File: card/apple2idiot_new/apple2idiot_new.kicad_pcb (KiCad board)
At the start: 2 copper layers, 167.6 x 77.5 mm, 10 parts, among them J1 Computer goes here, J2 Conn_02x02_Odd_Even, J3 Conn_01x04, J4 Conn_02x02_Odd_Even, J5 Conn_02x02_Odd_Even, J6 Conn_02x07_Odd_Even, U1 IDT7132, U2 ESP32-DEVKITC-32D

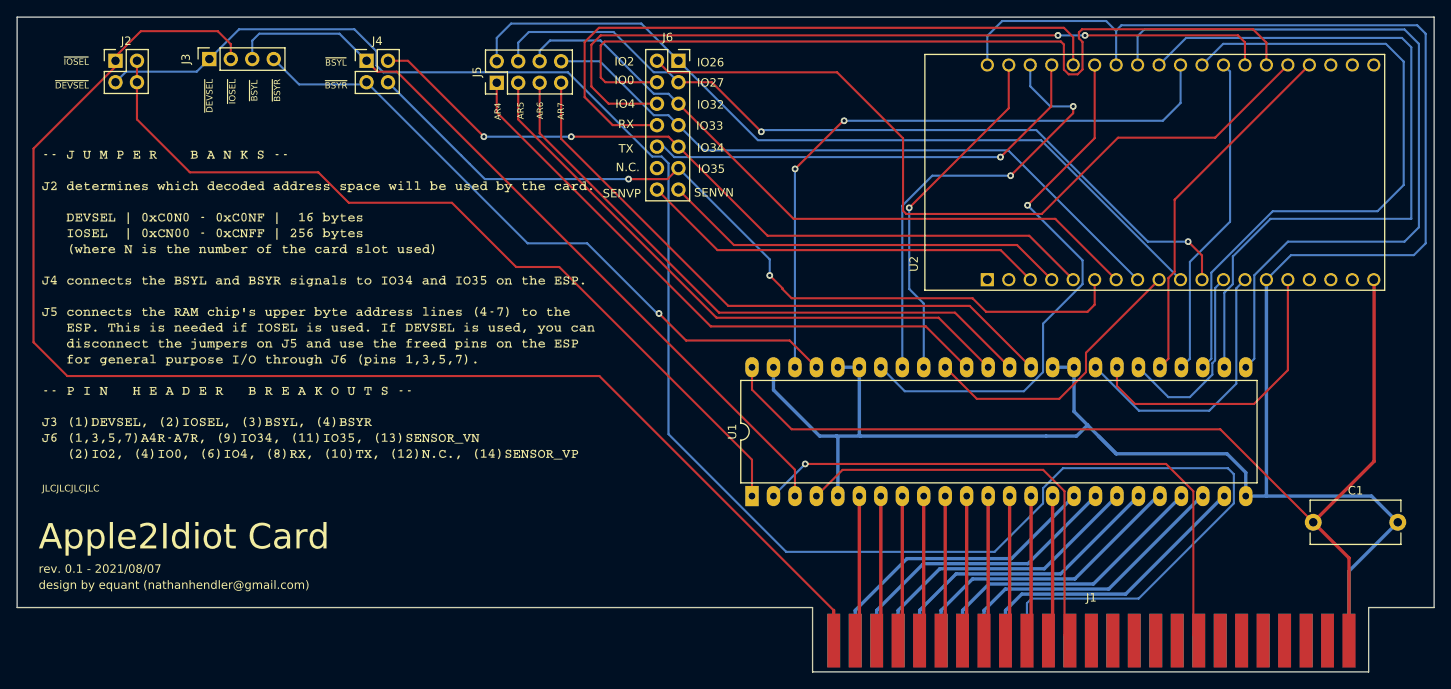
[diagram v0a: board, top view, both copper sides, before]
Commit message: Card work: Diode, no more DEVSEL support, A8-10 grounded, and more
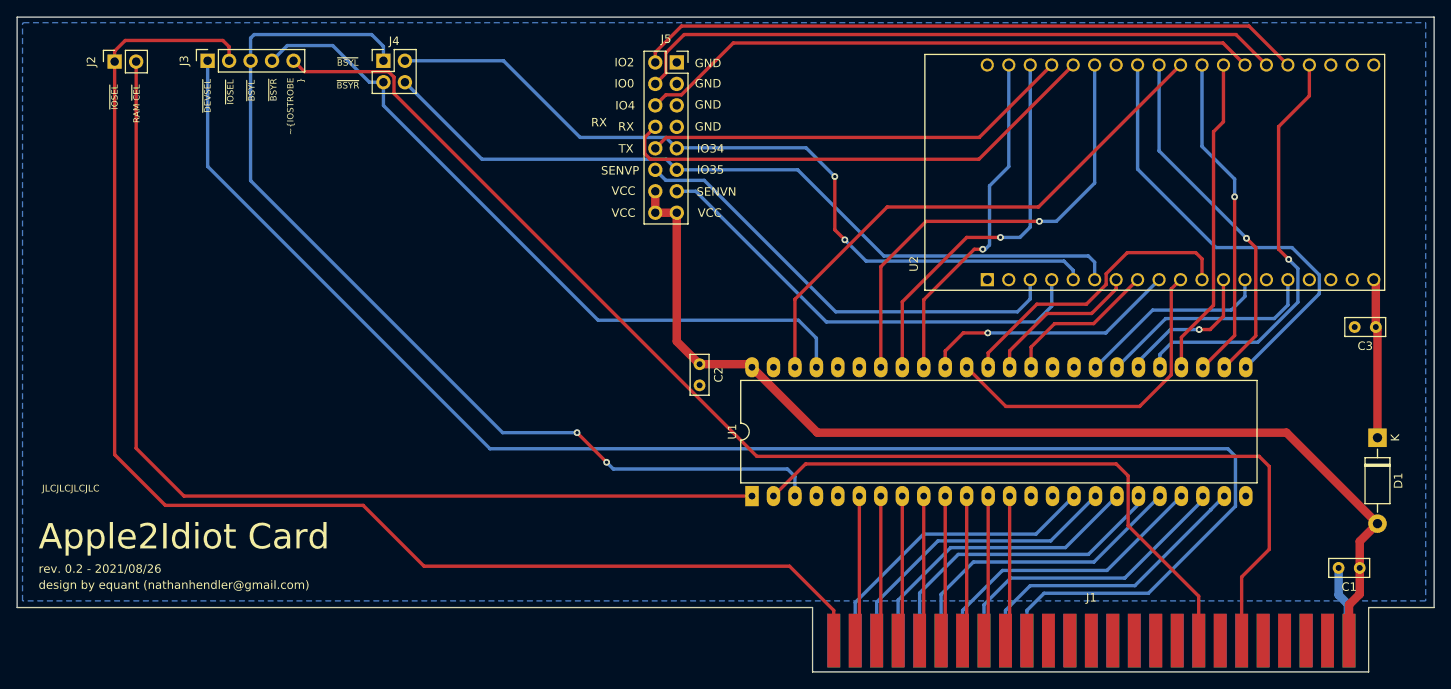
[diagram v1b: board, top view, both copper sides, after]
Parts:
- removed G***: LOGO, manual:manualFP
- removed J6: Conn_02x07_Odd_Even, Connector_PinSocket_2.54mm:PinSocket_2x07_P2.54mm_Vertical
- added C2: C, Capacitor_THT:C_Rect_L4.6mm_W2.0mm_P2.50mm_MKS02_FKP02, F.Cu at (154.4, 95.8)
- added C3: C, Capacitor_THT:C_Rect_L4.6mm_W2.0mm_P2.50mm_MKS02_FKP02, F.Cu at (234.4, 91.4)
- added D1: D, Diode_THT:D_DO-41_SOD81_P10.16mm_Horizontal, F.Cu at (234.6, 104.5)
- C1: footprint Capacitor_THT:C_Disc_D10.5mm_W5.0mm_P10.00mm -> Capacitor_THT:C_Rect_L4.6mm_W2.0mm_P2.50mm_MKS02_FKP02
- J1: value Computer goes here -> AppleIIBus
- J2: value Conn_02x02_Odd_Even -> Conn_02x01; footprint Connector_PinHeader_2.54mm:PinHeader_2x02_P2.54mm_Vertical -> Connector_PinSocket_2.54mm:PinSocket_1x02_P2.54mm_Vertical
- J3: value Conn_01x04 -> Conn_01x05; footprint Connector_PinSocket_2.54mm:PinSocket_1x04_P2.54mm_Vertical -> Connector_PinSocket_2.54mm:PinSocket_1x05_P2.54mm_Vertical
- J5: value Conn_02x02_Odd_Even -> Conn_02x08_Odd_Even; footprint Connector_PinHeader_2.54mm:PinHeader_2x04_P2.54mm_Vertical -> Connector_PinSocket_2.54mm:PinSocket_2x08_P2.54mm_Vertical
- moved J5 21.4 mm to (151.7, 60.1), turned to 0 degrees
- moved C1 7.71 mm to (232.5, 119.9), turned to 180 degrees
- moved J4 2.00 mm to (117.0, 59.9)
- moved J3 0.28 mm to (96.2, 59.9)
- moved J2 0.14 mm to (85.2, 60.0), turned to 90 degrees
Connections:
- J1 pad 10: /A8 -> Net-(J1-Pad10)
- J1 pad 11: /A9 -> Net-(J1-Pad11)
- J1 pad 12: /A10 -> Net-(J1-Pad12)
- J5 pad 1: /AR4 -> GND
- J5 pad 2: /IO26 -> /IO2
- J5 pad 3: /AR5 -> GND
- J5 pad 4: /IO27 -> /IO0
- J5 pad 5: /AR6 -> GND
- J5 pad 6: /IO32 -> /IO4
- J5 pad 7: /AR7 -> GND
- J5 pad 8: /IO33 -> /RX
- U1 pad 14: /A8 -> GND
- U1 pad 15: /A9 -> GND
- U1 pad 4: /A10 -> GND
- U2 pad 10: /IO26 -> /AR4
- U2 pad 11: /IO27 -> /AR5
- U2 pad 19: VCC -> Net-(C3-Pad1)
- U2 pad 7: /IO32 -> /AR6
- U2 pad 8: /IO33 -> /AR7
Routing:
- net GND: track 265.3 -> 9.11 mm
- net Net-(J1-Pad20): track 0.00 -> 158.4 mm
- net /IO27: track 97.6 -> 0.00 mm, vias 2 -> 0
- net /IO26: track 96.9 -> 0.00 mm
- net /IO32: track 81.7 -> 0.00 mm
- net /IO33: track 78.9 -> 0.00 mm
- net /AR7: track 73.4 -> 18.3 mm
- net /AR6: track 73.0 -> 18.7 mm
- net /A10: track 49.6 -> 0.00 mm
- net /DR6: track 88.4 -> 42.0 mm, vias 0 -> 1
- net /DR5: track 79.0 -> 38.9 mm, vias 0 -> 1
- net /DR7: track 92.6 -> 53.5 mm
- net /AR5: track 72.1 -> 35.4 mm
- net /DEVSEL: track 223.0 -> 187.6 mm
- net /AR4: track 71.6 -> 39.4 mm
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- added copper zone on B.Cu, net GND
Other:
- board text added: "GND"
- board text added: "RAM ~CEL"
- board text added: "VCC"
- board text added: "rev. 0.2 - 2021/08/26"
- board text added: "~IOSTROBE"
- board text removed: "AR4"
- board text removed: "AR5"
- board text removed: "AR6"
- board text removed: "AR7"
- board text removed: "IO26"
- board text removed: "IO27"
- board text removed: "IO32"
- board text removed: "IO33"
- board text removed: "N.C."
- board text removed: "rev. 0.1 - 2021/08/07"

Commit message: Rev 0.2 card changes, and staging a cc65 weather repo
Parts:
- moved U2 15.5 mm to (192.7, 73.1)
- moved J5 9.71 mm to (142.0, 59.6)
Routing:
- net /DR4: track 37.8 -> 79.8 mm
- net /DR5: track 38.9 -> 76.1 mm, vias 1 -> 0
- net /DR6: track 42.0 -> 75.8 mm, vias 1 -> 0
- net /AR4: track 39.4 -> 14.4 mm
- net /BSYL: track 116.3 -> 140.0 mm, vias 2 -> 0
- net /AR5: track 35.4 -> 14.4 mm
- net /DR7: track 53.5 -> 71.3 mm
- net /IO35: track 92.5 -> 75.8 mm
- net RWR: track 65.1 -> 81.5 mm
- net /AR3: track 30.7 -> 14.4 mm, vias 1 -> 0
- net /IO34: track 94.2 -> 77.9 mm, vias 2 -> 0
- net /DR3: track 50.9 -> 36.7 mm, vias 1 -> 0
- net /DR1: track 26.3 -> 12.3 mm
- net /AR0: track 55.3 -> 41.9 mm, vias 1 -> 0
- net Net-(C3-Pad1): track 18.9 -> 31.9 mm
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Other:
- board text removed: "JLCJLCJLCJLC"
